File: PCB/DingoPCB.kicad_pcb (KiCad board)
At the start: 2 copper layers, 80 x 40 mm, 23 parts, among them J1 BATT(~15V), J10 BATT CHECK, J11 1935776, J12 1935776, J13 1935776, J14 1935776, J15 TEMP1, J16 TEMP2, J17 TEMP3, J18 TEMP4, J19 FAN1, J2 PWR1, J20 FAN2, J3 PWR2, J4 PWR3, J5 PWR4, J6 12VIN, J7 5VIN, J8 1935776, J9 1935776

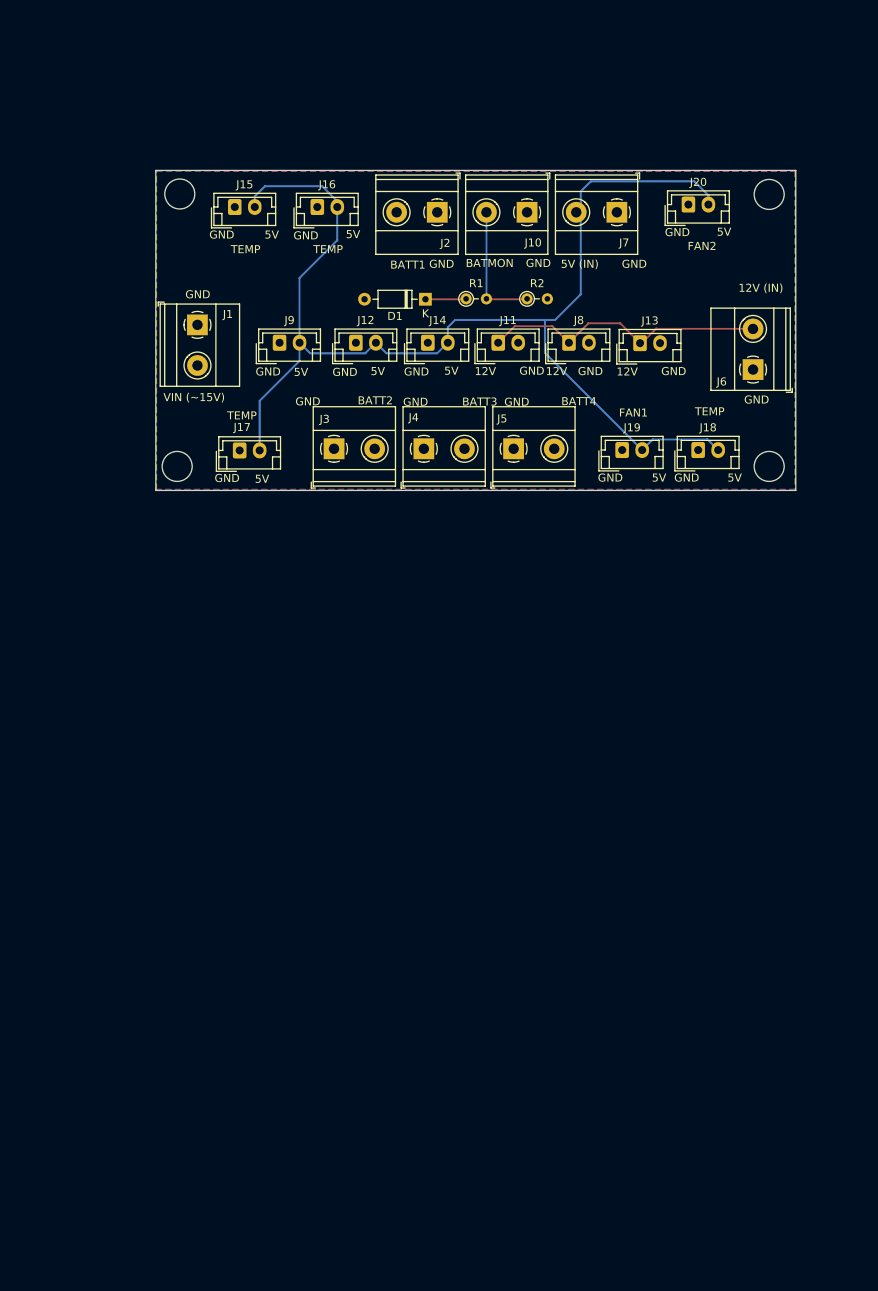
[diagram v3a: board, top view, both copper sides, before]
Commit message: Adding updated servo carriers
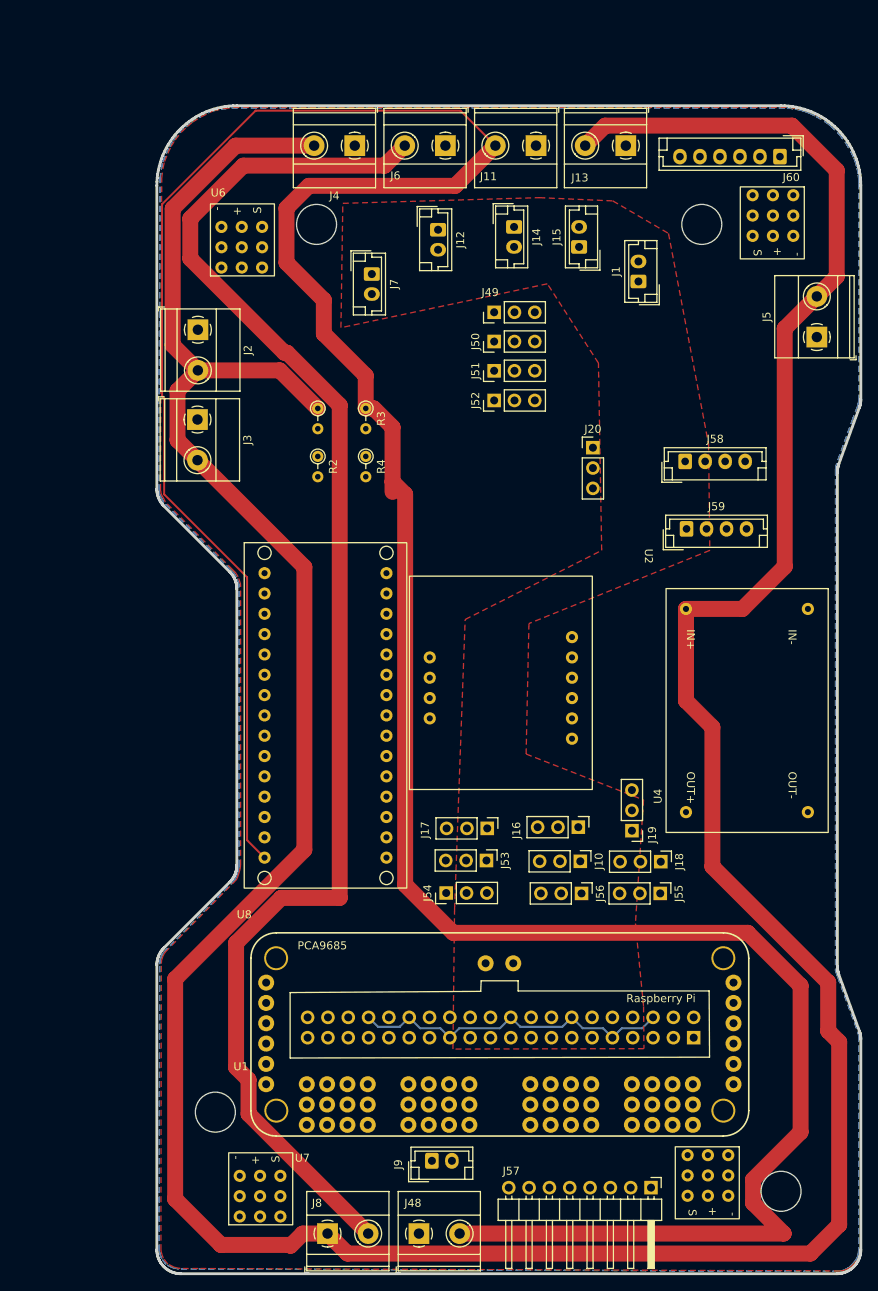
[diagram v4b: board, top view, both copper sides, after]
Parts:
- removed D1: 1N5711, Diode_THT:D_DO-35_SOD27_P7.62mm_Horizontal
- added J21: Raspberry_Pi_Conn, Connector_PinHeader_2.54mm:PinHeader_2x20_P2.54mm_Vertical, B.Cu at (85.0, 127.7)
- added J48: STOP SW+, TerminalBlock_Phoenix:TerminalBlock_Phoenix_MKDS-1,5-2-5.08_1x02_P5.08mm_Horizontal, F.Cu at (50.6, 152.1)
- added J49: AUXSRV1, Connector_PinHeader_2.54mm:PinHeader_1x03_P2.54mm_Vertical, F.Cu at (60.0, 37.0)
- added J50: AUXSRV2, Connector_PinHeader_2.54mm:PinHeader_1x03_P2.54mm_Vertical, F.Cu at (60.0, 40.6)
- added J51: AUXSRV3, Connector_PinHeader_2.54mm:PinHeader_1x03_P2.54mm_Vertical, F.Cu at (60.0, 44.3)
- added J52: AUXSRV4, Connector_PinHeader_2.54mm:PinHeader_1x03_P2.54mm_Vertical, F.Cu at (60.0, 48.0)
- added J53: PCA9685SCL, Connector_PinHeader_2.54mm:PinHeader_1x03_P2.54mm_Vertical, F.Cu at (59.1, 105.5)
- added J54: LCDDIN, Connector_PinHeader_2.54mm:PinHeader_1x03_P2.54mm_Vertical, F.Cu at (54.1, 109.6)
- added J55: LCDCLK, Connector_PinHeader_2.54mm:PinHeader_1x03_P2.54mm_Vertical, F.Cu at (80.8, 109.6)
- added J56: LCDCS, Connector_PinHeader_2.54mm:PinHeader_1x03_P2.54mm_Vertical, F.Cu at (71.0, 109.6)
- added J57: LCDHEADER, Connector_PinHeader_2.54mm:PinHeader_1x08_P2.54mm_Horizontal, F.Cu at (79.7, 146.4)
- added J58: PII2CAUX, Connector_JST:JST_EH_B4B-EH-A_1x04_P2.50mm_Vertical, F.Cu at (83.9, 55.6)
- added J59: NANOI2CAUX, Connector_JST:JST_EH_B4B-EH-A_1x04_P2.50mm_Vertical, F.Cu at (84.1, 64.1)
- added J60: Sonar_Connectors, Connector_JST:JST_EH_B6B-EH-A_1x06_P2.50mm_Vertical, F.Cu at (95.8, 17.5)
- added R3: R, Resistor_THT:R_Axial_DIN0204_L3.6mm_D1.6mm_P2.54mm_Vertical, F.Cu at (44.0, 49.0)
- added R4: R, Resistor_THT:R_Axial_DIN0204_L3.6mm_D1.6mm_P2.54mm_Vertical, F.Cu at (44.0, 55.0)
- added U1: ~, PCA9685:Adafruit PCA9685 rev C, F.Cu at (32.8, 136.8)
- added U2: ~, Inductor_THT:DFR0831, F.Cu at (78.9, 71.5)
- added U3: BRSERVOS, Connector:Three_Servo_Footprint, F.Cu at (81.7, 139.8)
- added U4: ~, Module:Adafruit BNO055, F.Cu at (77.4, 97.9)
- added U5: FRSERVOS, Connector:Three_Servo_Footprint, F.Cu at (89.8, 19.8)
- added U6: FLSERVOS, Connector:Three_Servo_Footprint, F.Cu at (33.6, 33.9)
- added U7: BLSERVOS, Connector:Three_Servo_Footprint, F.Cu at (35.9, 152.6)
- added U8: ~, Module:Arduino_Nano_ESP32, F.Cu at (28.8, 112.8)
- J1: value BATT(~15V) -> FANF; footprint TerminalBlock_Phoenix:TerminalBlock_Phoenix_MKDS-1,5-2-5.08_1x02_P5.08mm_Horizontal -> Connector_JST:JST_EH_B2B-EH-A_1x02_P2.50mm_Vertical
- J10: value BATT CHECK -> PCA9685SDA; footprint TerminalBlock_Phoenix:TerminalBlock_Phoenix_MKDS-1,5-2-5.08_1x02_P5.08mm_Horizontal -> Connector_PinHeader_2.54mm:PinHeader_1x03_P2.54mm_Vertical
- J11: value 1935776 -> BUCKOUT; footprint Connector_JST:JST_EH_B2B-EH-A_1x02_P2.50mm_Vertical -> TerminalBlock_Phoenix:TerminalBlock_Phoenix_MKDS-1,5-2-5.08_1x02_P5.08mm_Horizontal
- J12: value 1935776 -> 5VAUX2
- J13: value 1935776 -> BUCKIN; footprint Connector_JST:JST_EH_B2B-EH-A_1x02_P2.50mm_Vertical -> TerminalBlock_Phoenix:TerminalBlock_Phoenix_MKDS-1,5-2-5.08_1x02_P5.08mm_Horizontal
- J14: value 1935776 -> 5VAUX3
- J15: value TEMP1 -> 5VAUX4
- J16: value TEMP2 -> BNO055SDA; footprint Connector_JST:JST_EH_B2B-EH-A_1x02_P2.50mm_Vertical -> Connector_PinHeader_2.54mm:PinHeader_1x03_P2.54mm_Vertical
- J17: value TEMP3 -> BNO055SCL; footprint Connector_JST:JST_EH_B2B-EH-A_1x02_P2.50mm_Vertical -> Connector_PinHeader_2.54mm:PinHeader_1x03_P2.54mm_Vertical
- J18: value TEMP4 -> LCDDS; footprint Connector_JST:JST_EH_B2B-EH-A_1x02_P2.50mm_Vertical -> Connector_PinHeader_2.54mm:PinHeader_1x03_P2.54mm_Vertical
- J19: value FAN1 -> LCDRST; footprint Connector_JST:JST_EH_B2B-EH-A_1x02_P2.50mm_Vertical -> Connector_PinHeader_2.54mm:PinHeader_1x03_P2.54mm_Vertical
- J20: value FAN2 -> LCDBL; footprint Connector_JST:JST_EH_B2B-EH-A_1x02_P2.50mm_Vertical -> Connector_PinHeader_2.54mm:PinHeader_1x03_P2.54mm_Vertical
- J6: value 12VIN -> BATTIN
- J7: value 5VIN -> 5VAUX1; footprint TerminalBlock_Phoenix:TerminalBlock_Phoenix_MKDS-1,5-2-5.08_1x02_P5.08mm_Horizontal -> Connector_JST:JST_EH_B2B-EH-A_1x02_P2.50mm_Vertical
- J8: value 1935776 -> MSTR SW; footprint Connector_JST:JST_EH_B2B-EH-A_1x02_P2.50mm_Vertical -> TerminalBlock_Phoenix:TerminalBlock_Phoenix_MKDS-1,5-2-5.08_1x02_P5.08mm_Horizontal
- J9: value 1935776 -> FANR
- moved J8 115.4 mm to (39.2, 152.1)
- moved J9 104.0 mm to (52.3, 143.1)
- moved J16 84.1 mm to (70.6, 101.3), turned to -90 degrees
- moved J10 81.4 mm to (70.8, 105.6), turned to -90 degrees
- moved J17 56.5 mm to (59.2, 101.5), turned to -90 degrees
- moved J1 55.4 mm to (78.1, 33.1), turned to 90 degrees
- moved J18 51.7 mm to (80.9, 105.7), turned to -90 degrees
- moved J19 47.6 mm to (77.3, 101.8), turned to 180 degrees
- moved J6 47.6 mm to (53.9, 16.2), turned to 180 degrees
- moved J15 43.3 mm to (70.7, 28.8), turned to 90 degrees
- moved J5 40.4 mm to (100.4, 40.1), turned to 90 degrees
- moved J4 38.9 mm to (42.6, 16.2), turned to 180 degrees
- moved J2 33.3 mm to (23.0, 39.2), turned to -90 degrees
- moved R2 32.7 mm to (38.0, 55.0), turned to -90 degrees
- moved J20 32.7 mm to (72.4, 53.9)
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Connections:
- J1 pad 2: +15V -> +5V
- J10 pad 1: GND -> NANOSDA
- J10 pad 2: Net-(J10-Pin_2) -> PCA9685SDA
- J11 pad 1: +12V -> GND
- J11 pad 2: GND -> +7.5V
- J13 pad 1: +12V -> GND
- J13 pad 2: GND -> +15V
- J16 pad 1: GND -> NANOSDA
- J16 pad 2: +5V -> BNO055SDA
- J17 pad 1: GND -> NANOSCL
- J17 pad 2: +5V -> BNO055SCL
- J18 pad 1: GND -> NANOLCDDS
- J18 pad 2: +5V -> LCDDS
- J19 pad 1: GND -> NANOLCDRST
- J19 pad 2: +5V -> LCDRST
- J20 pad 1: GND -> NANOLCDBL
- J20 pad 2: +5V -> LCDBL
- J6 pad 2: +12V -> +VDC
- J8 pad 1: +12V -> +15V
- J8 pad 2: GND -> +VDC
- R1 pad 1: Net-(D1-K) -> +15V
- R1 pad 2: Net-(J10-Pin_2) -> NANOA0
- R2 pad 1: Net-(J10-Pin_2) -> NANOA0
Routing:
- net +15V: track 0.00 -> 452.4 mm
- net +7.5V: track 0.00 -> 387.4 mm
- net +VDC: track 0.00 -> 181.9 mm
- net +5V: track 152.2 -> 0.00 mm
- net NANOA1: track 0.00 -> 42.9 mm
- net GND: track 0.00 -> 41.7 mm
- net NANOA0: track 0.00 -> 36.8 mm
- net +12V: track 36.4 -> 0.00 mm
- net Net-(J10-Pin_2): track 16.1 -> 0.00 mm
- net Net-(D1-K): track 4.88 -> 0.00 mm
- added copper zone on F.Cu, net +5V
- added copper zone on In2.Cu, net +5V
- added copper zone on F.Cu, net +VSW
- added copper zone on In1.Cu, net +VSW
- removed copper zone on F.Cu, net +15V
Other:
- board size 80 x 40 mm -> 88 x 146 mm
- copper layers 2 -> 4
- board text added: "PCA9685"
- board text added: "Raspberry Pi"
- board text removed: "12V"
- board text removed: "12V (IN)"
- board text removed: "5V"
- board text removed: "5V (IN)"
- board text removed: "BATMON"
- board text removed: "BATT1"
- board text removed: "BATT2"
- board text removed: "BATT3"
- board text removed: "BATT4"
- board text removed: "FAN1"
- board text removed: "FAN2"
- board text removed: "GND"
- board text removed: "TEMP"
- board text removed: "UNOFFICIAL DINGO PCB"
- board text removed: "VIN (~15V)"
